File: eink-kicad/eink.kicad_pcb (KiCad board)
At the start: 2 copper layers, 34.3 x 68.6 mm, 83 parts, among them J1 0R, P1 CONN_1, P10 CONN_1, P11 CONN_1, P12 CONN_1, P13 CONN_1, P14 CONN_1, P15 CONN_1, P16 CONN_1, P17 CONN_1, P18 CONN_1, P19 CONN_1, P2 CONN_1, P20 CONN_1, P21 CONN_1, P22 CONN_1, P23 CONN_1, P24 CONN_1, P25 CONN_1, P26 CONN_1, P27 CONN_1, P28 CONN_1, P29 CONN_1, P3 CONN_1, P30 CONN_1, P31 CONN_1, P32 CONN_1, P33 CONN_1, P34 CONN_1, P35 CONN_1, P36 CONN_1, P37 CONN_1, P38 CONN_1, P39 CONN_1, P4 CONN_1, P40 CONN_1, P41 CONN_1, P42 CONN_1, P43 CONN_1, P5 CONN_1, P6 CONN_1, P7 CONN_1, P8 CONN_1, P9 CONN_1, Q1 MOS_P, U1 LT1945, U2 78L15, U3 79L15, U4 LM358, U5 ED060SC4V2-FPC

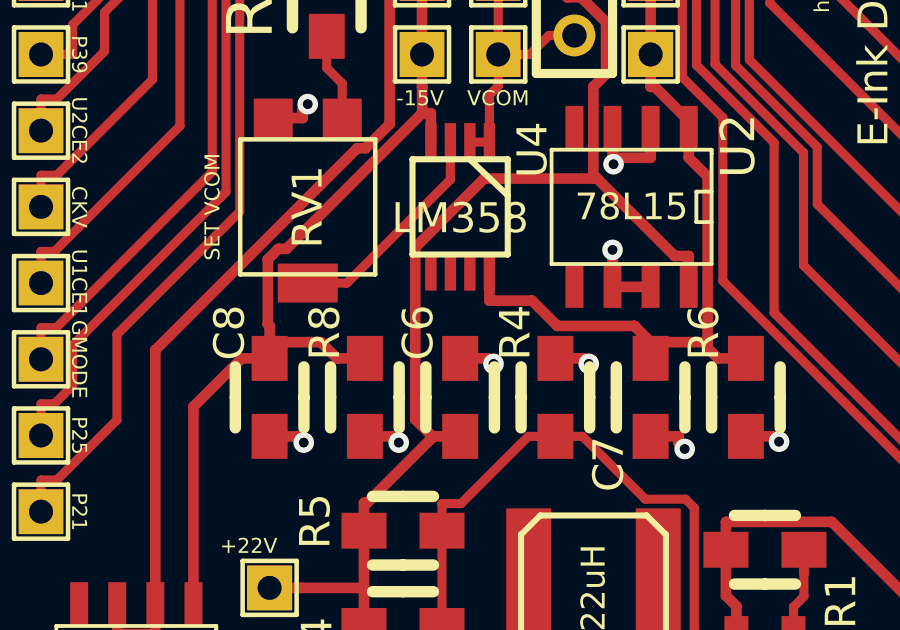
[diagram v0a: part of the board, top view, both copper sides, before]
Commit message: Terminate the LM358's other op-amp.
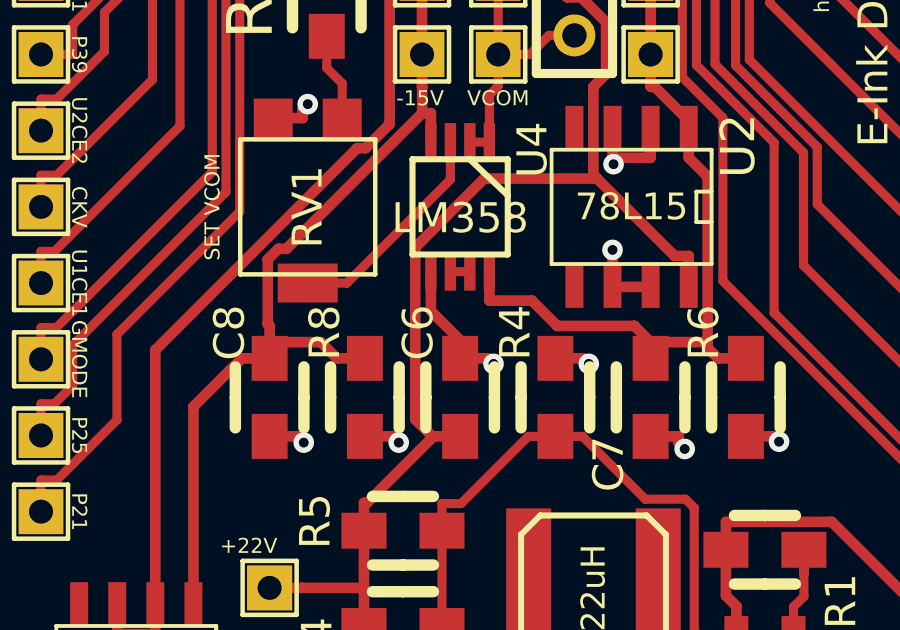
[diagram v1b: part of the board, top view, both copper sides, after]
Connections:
- U4 pad 5: (no net) -> GND
- U4 pad 6: (no net) -> N-0000032
- U4 pad 7: (no net) -> N-0000032
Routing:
- net GND: track 33.2 -> 36.5 mm
- net N-0000032: track 0.00 -> 0.65 mm

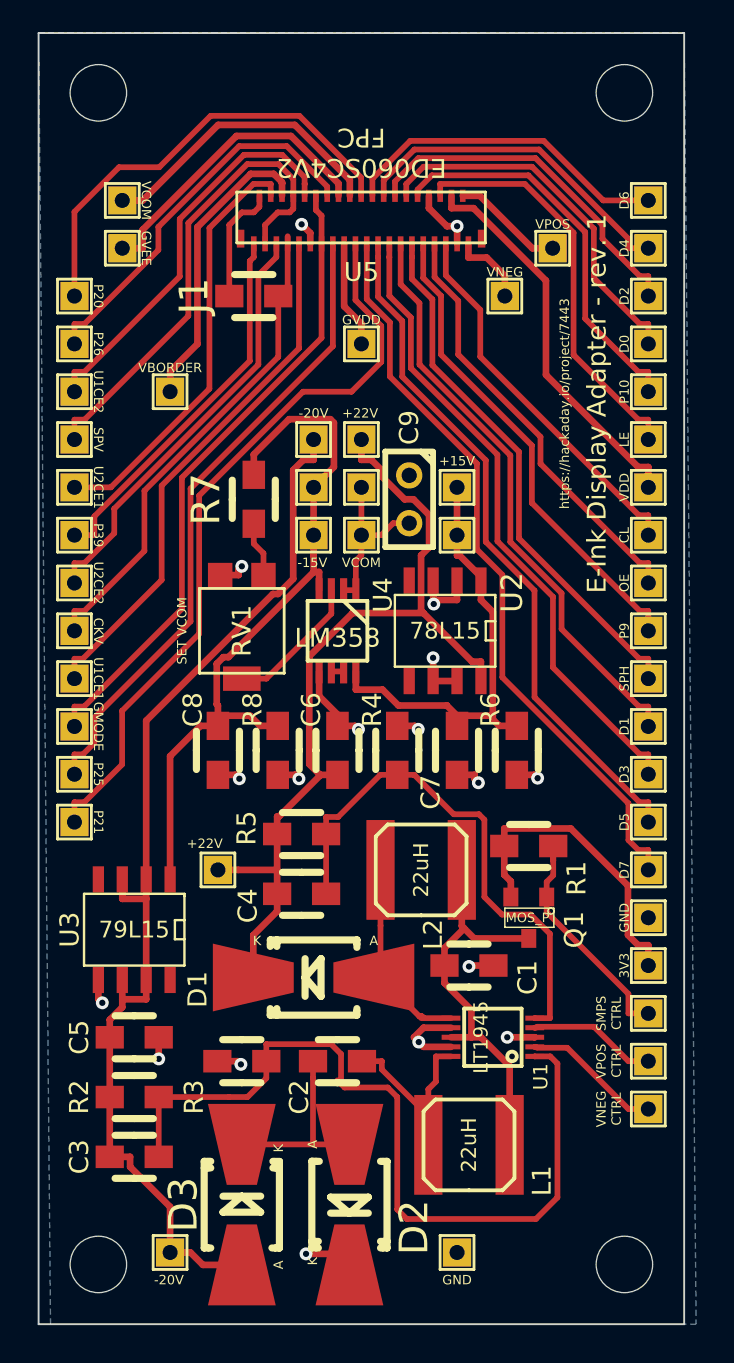
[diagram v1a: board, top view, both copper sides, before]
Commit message: Partially rerun routing to fix some DRC violations (caused by manual routing :/ ).
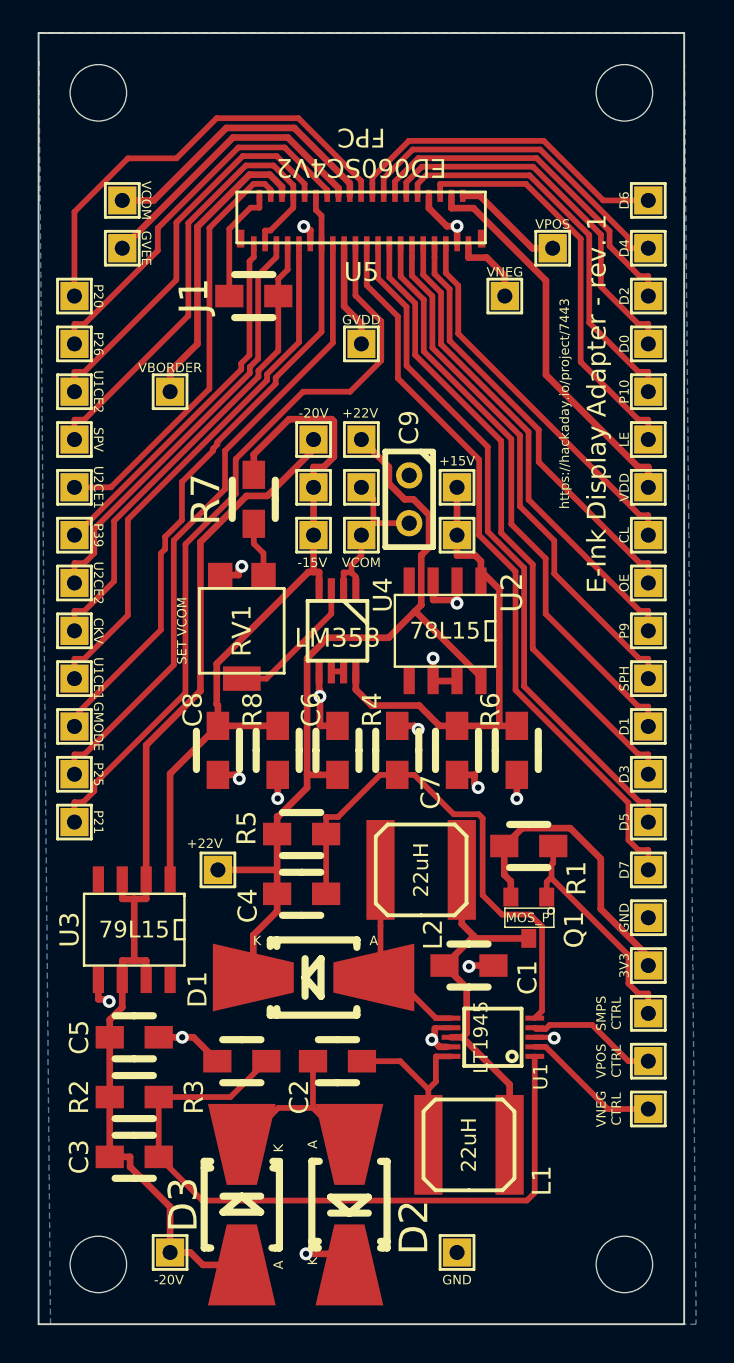
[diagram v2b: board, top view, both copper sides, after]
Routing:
- net /NFB1: track 44.1 -> 38.0 mm
- net /+15V: track 24.0 -> 25.0 mm
- net /+3.3V: track 16.7 -> 15.8 mm
- net GND: track 36.5 -> 35.6 mm, vias 18 -> 17
- net /SMPS_VIN: track 21.6 -> 20.7 mm
- net /SW1: track 10.7 -> 9.81 mm
- net /FB2: track 28.1 -> 27.2 mm
- net /GVEE: track 16.2 -> 15.4 mm
- net /P39: track 20.0 -> 19.5 mm
- net /+22V: track 46.6 -> 46.1 mm
- net N-0000016: track 9.04 -> 9.56 mm

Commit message: Fix FPC connector pinout and turn it around to face edge.
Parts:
- removed MH1, MH2, MH3, MH4: MountingHole_3mm_RevA_Date21Jun2010, MountingHole_3mm_RevA_Date21Jun2010
- removed P41, P42, P43, P8: CONN_1, SIL-1
- U2: value 78L15 -> LM358; footprint 78LxxA -> MSOP_8
- U3: value 79L15 -> 78L15; footprint 79LxxA -> 78LxxA
- U4: value LM358 -> 79L15; footprint MSOP_8 -> 79LxxA
- moved P27 44.9 mm to (109.2, 111.8)
- moved P25 35.6 mm to (109.2, 109.2)
- moved P26 35.6 mm to (109.2, 73.7)
- moved P23 30.5 mm to (109.2, 106.7)
- moved P24 30.5 mm to (109.2, 76.2)
- moved P28 30.5 mm to (78.7, 76.2)
- moved P31 25.5 mm to (78.7, 101.6), turned to 270 degrees
- moved P21 25.4 mm to (109.2, 104.1)
- moved P22 25.4 mm to (109.2, 78.7)
- moved U3 22.9 mm to (98.4, 96.5)
- moved P32 22.9 mm to (78.7, 81.3)
- moved P19 20.3 mm to (109.2, 101.6)
- moved P20 20.3 mm to (109.2, 81.3)
- moved U4 19.2 mm to (81.9, 112.4)
- moved P33 17.8 mm to (78.7, 99.1)
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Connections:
- C9 pad 2: N-0000016 -> /VCOM
- P29 pad 1: /VCOM -> /GVDD
- P30 pad 1: /GVDD -> /P25
- P31 pad 1: /GVEE -> /P26
- P32 pad 1: /P25 -> /GMODE
- P33 pad 1: /P26 -> /U1CE2
- P34 pad 1: /GMODE -> /U1CE1
- P35 pad 1: /U1CE2 -> /SPV
- P36 pad 1: /U1CE1 -> /CKV
- P37 pad 1: /SPV -> /VBORDER
- P38 pad 1: /CKV -> /U2CE2
- P39 pad 1: /VBORDER -> /U2CE1
- P40 pad 1: /U2CE2 -> /P39
- RV1 pad 2: N-0000047 -> N-0000025
- TP6 pad 1: N-0000016 -> /VCOM
- U2 pad 4: (no net) -> /-15V
- U2 pad 5: (no net) -> N-0000025
- U3 pad VI: /-20V -> /+22V
- U3 pad VO: /-15V -> /+15V
- U4 pad 4: /-15V -> (no net)
- U4 pad 8: /+15V -> (no net)
- U5 pad 24: /GVEE -> /-20V
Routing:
- net /D6: track 17.7 -> 39.8 mm
- net /D7: track 39.8 -> 19.1 mm
- net /P21: track 39.8 -> 19.9 mm
- net /D4: track 18.1 -> 37.0 mm
- net /P20: track 23.9 -> 42.6 mm
- net /D5: track 36.9 -> 19.1 mm
- net /GVEE: track 15.4 -> 0.00 mm
- net /D2: track 18.9 -> 34.2 mm
- net /P25: track 34.2 -> 19.8 mm
- net /D3: track 34.2 -> 19.8 mm
- net /VCOM: track 15.6 -> 29.1 mm
- net /P26: track 20.3 -> 31.7 mm
- net /D0: track 20.0 -> 31.4 mm
- net /GVDD: track 5.69 -> 16.6 mm
- net /GMODE: track 33.7 -> 23.0 mm
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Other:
- net class logic added: clearance 0.1524, trace_width 0.3048, via_dia 0.6858, via_drill 0.3302
- board text removed: "GVEE"

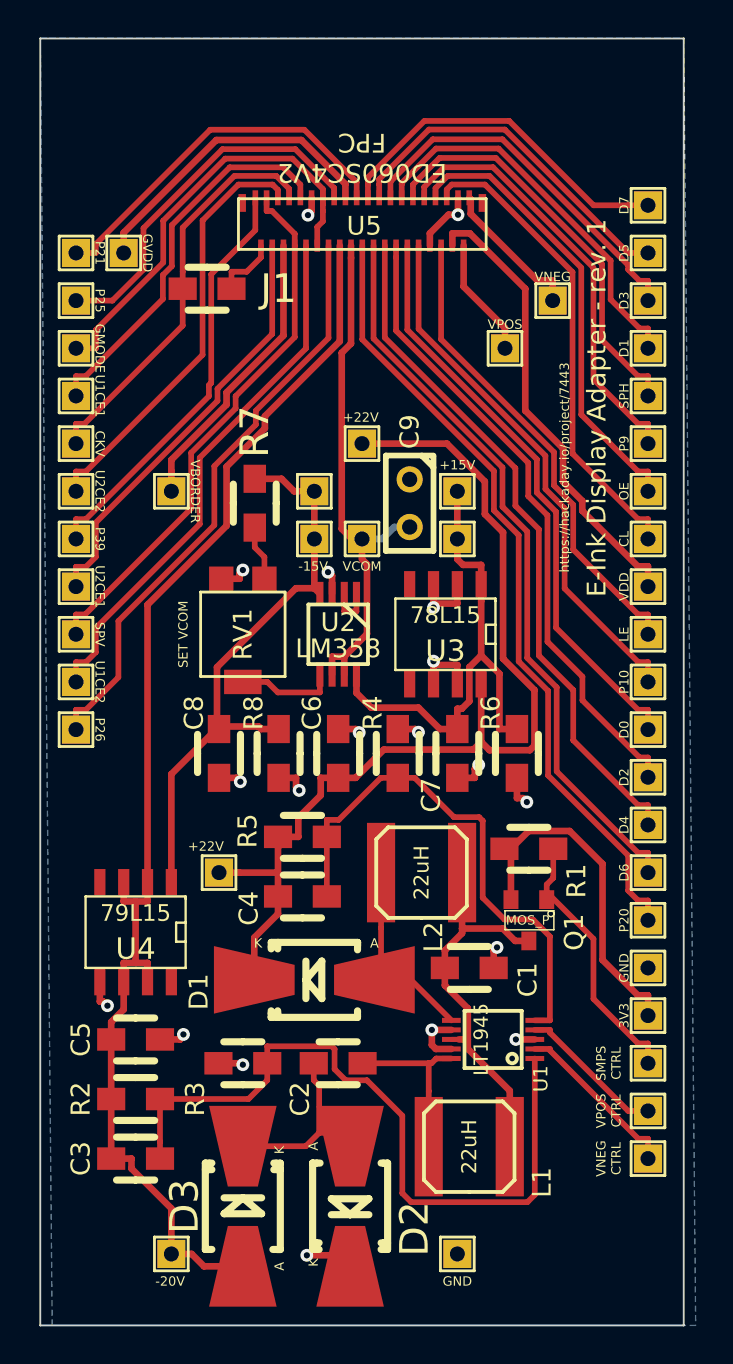
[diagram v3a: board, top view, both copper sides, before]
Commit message: New version of board for new version of KiCad :)
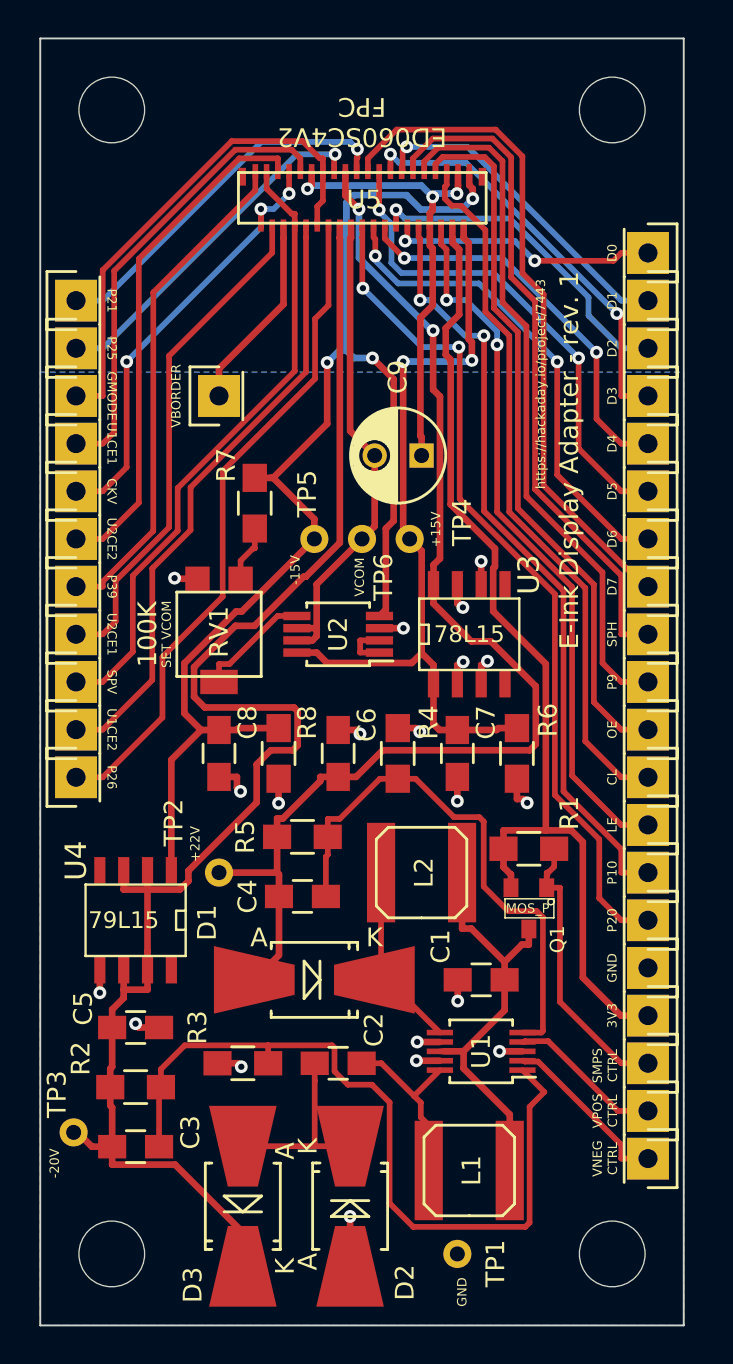
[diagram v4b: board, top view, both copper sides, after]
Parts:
- removed J1: 0R, Resistor_SMD0805_HandSoldering_RevA_Date21Jun2010
- removed P10, P11, P12, P29, P34, P6, P7, P9: CONN_1, SIL-1
- added REF**: MountingHole_3-5mm, Mounting_Holes:MountingHole_3-5mm, F.Cu at (80.6, 129.5)
- added REF**: MountingHole_3-5mm, Mounting_Holes:MountingHole_3-5mm, F.Cu at (107.3, 129.5)
- added REF**: MountingHole_3-5mm, Mounting_Holes:MountingHole_3-5mm, F.Cu at (107.3, 68.6)
- added REF**: MountingHole_3-5mm, Mounting_Holes:MountingHole_3-5mm, F.Cu at (80.6, 68.6)
- added eP34: CONN_1, Pin_Headers:Pin_Header_Straight_1x01, F.Cu at (78.7, 86.4)
- C1, C2, C3, C4, C5, C6, C7, C8: footprint Capacitor_SMD0805_HandSoldering_RevA_Date21Jun2010 -> Capacitors_SMD:C_0805_HandSoldering
- C9: footprint C1 -> Capacitors_ThroughHole:C_Radial_D5_L6_P2.5
- D1, D2, D3: footprint Diode-Universal-SMB-SMC_Handsoldering_RevA_27July2010 -> Diodes_SMD:SMB-SMC_Universal_Handsoldering
- L1, L2: footprint SELF-WE-TPC_M -> Inductors:SELF-WE-TPC_M
- P1, P13, P14, P15, P16, P17, P18, P19, P2, P20, P21, P22, P23, P24, P25, P26, P27, P28, P3, P30, P31, P32, P33, P35, P36, P37, P38, P39, P4, P40, P5: footprint SIL-1 -> Pin_Headers:Pin_Header_Straight_1x01
- Q1: footprint IRLML6402 -> eink-footprints:IRLML6402
- R1, R2, R3, R4, R5, R6, R7, R8: footprint Resistor_SMD0805_HandSoldering_RevA_Date21Jun2010 -> Resistors_SMD:R_0805_HandSoldering
- RV1: footprint Bourns_3314G-1 -> eink-footprints:Bourns_3314G-1
- TP1, TP2, TP3, TP4, TP5, TP6: footprint SIL-1 -> Measurement_Points:Measurement_Point_Round-TH_Small
- U1: footprint MSOP10-0.5 -> Housings_SSOP:MSOP-10_3x3mm_Pitch0.5mm
- U2: footprint MSOP_8 -> Housings_SSOP:MSOP-8_3x3mm_Pitch0.65mm
- U3: footprint 78LxxA -> eink-footprints:78LxxA
- U4: footprint 79LxxA -> eink-footprints:79LxxA
- U5: footprint FH26-39S-0.3SHW -> eink-footprints:FH26-39S-0.3SHW
- moved P19 25.4 mm to (109.2, 76.2)
- moved P21 22.9 mm to (109.2, 81.3)
- moved P23 20.3 mm to (109.2, 86.4)
- moved P26 20.3 mm to (109.2, 94.0)
- moved P25 17.8 mm to (109.2, 91.4)
- moved P13 12.7 mm to (109.2, 104.1)
- moved P16 12.7 mm to (109.2, 99.1)
- moved P18 12.7 mm to (109.2, 96.5)
- moved P24 12.7 mm to (109.2, 88.9)
- moved P15 12.7 mm to (109.2, 101.6)
- moved P14 10.2 mm to (109.2, 106.7)
- moved P17 10.2 mm to (109.2, 109.2)
- moved TP3 8.31 mm to (78.6, 123.1)
- moved P37 5.68 mm to (86.4, 83.8)
- moved P22 5.08 mm to (109.2, 83.8)
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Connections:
- U5 pad 1: /VNEG -> /-15V
- U5 pad 2: /VPOS -> /+15V
- U5 pad 23: /GVDD -> /+22V
- U5 pad 38: N-0000030 -> /CKV
- U5 pad 4: /VDD -> /+3.3V
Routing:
- net /-15V: track 31.9 -> 72.6 mm, vias 0 -> 3
- net /+3.3V: track 18.5 -> 54.2 mm
- net /VDD: track 24.7 -> 0.00 mm
- net GND: track 35.0 -> 52.8 mm, vias 19 -> 23
- net /D0: track 31.4 -> 14.4 mm, vias 0 -> 2
- net /D7: track 19.1 -> 36.0 mm
- net /GVDD: track 16.6 -> 0.00 mm
- net /D2: track 34.2 -> 17.9 mm, vias 0 -> 1
- net /+15V: track 26.8 -> 42.8 mm, vias 0 -> 2
- net /D4: track 37.0 -> 21.3 mm, vias 0 -> 2
- net /SPH: track 22.1 -> 36.1 mm
- net /P9: track 23.1 -> 37.1 mm
- net /OE: track 24.3 -> 38.1 mm
- net /-20V: track 68.9 -> 82.6 mm
- net /D6: track 39.8 -> 26.1 mm, vias 0 -> 2
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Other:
- net class power-gnd added: clearance 0.1524, trace_width 0.3556, via_dia 0.6858, via_drill 0.3302
- board text removed: "GVDD"
- board text removed: "VDD"
- board text removed: "VNEG"
- board text removed: "VPOS"
